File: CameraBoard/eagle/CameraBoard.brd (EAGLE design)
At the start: 101.6 x 76.2 mm, 86 parts, among them Q1 SI7465DP-T1-E3, Q2 BVSS123LT1G, Q3 BSS84, U1 MP26124GR-Z, U2 TPS63070, U3 LM2678SD-12/NOPB, U4 TS5A3159ADBVR, U5 ICM7242IBAZ-SMD, U6 H11F1SR2M, U7 H11F1SR2M, U8 SN74LVC1G17DCKR

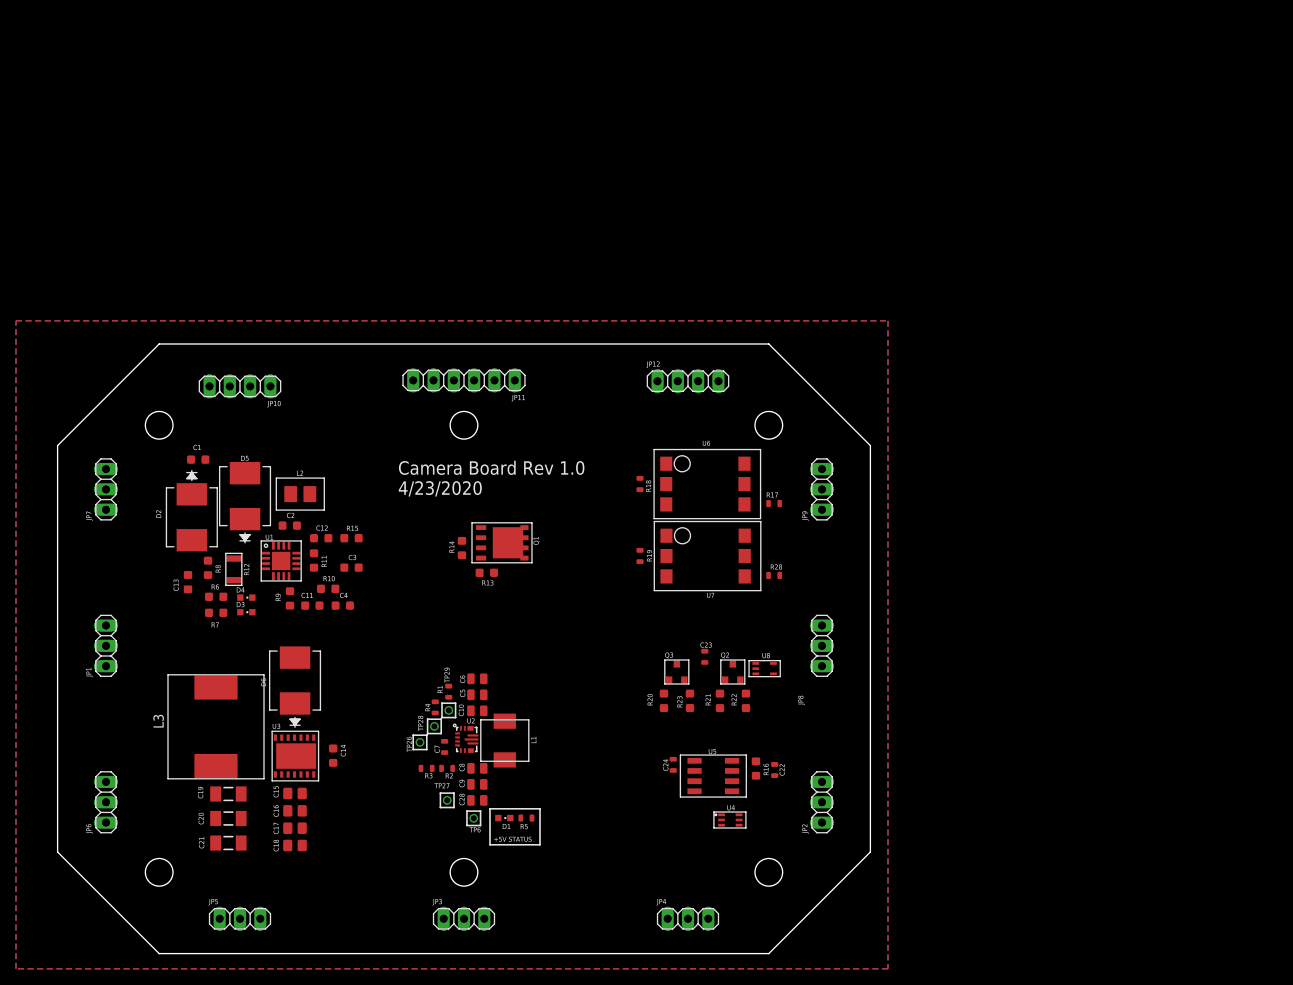
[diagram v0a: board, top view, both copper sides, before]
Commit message: finished board layout before routing
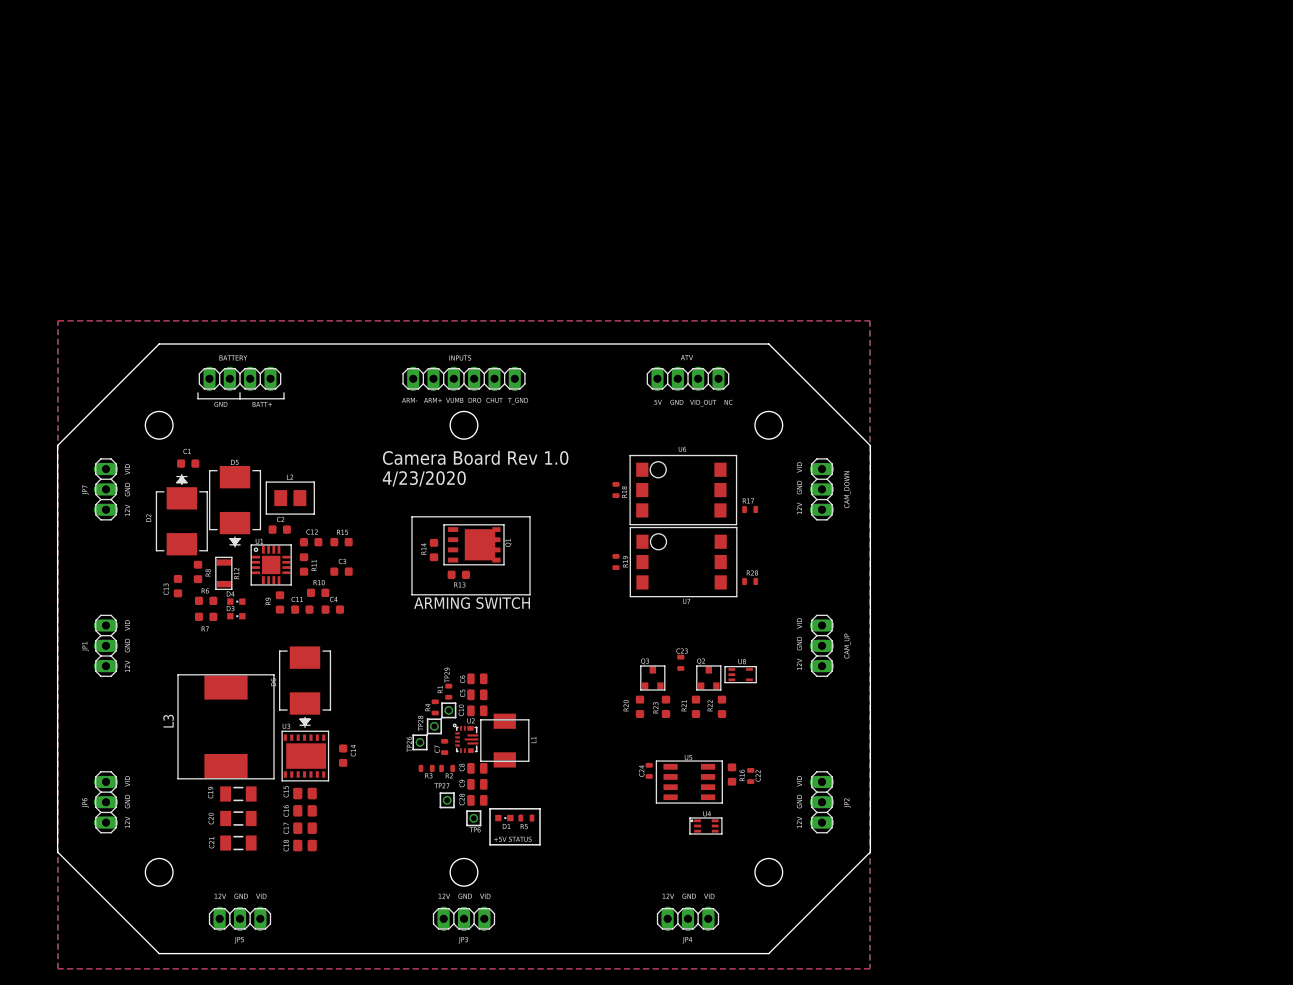
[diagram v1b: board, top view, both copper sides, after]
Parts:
- removed JP10, JP12: (no value), pinhead:1X04
- removed JP11: (no value), pinhead:1X06
- added ATV, BATTERY: (no value), pinhead:1X04
- added INPUTS: (no value), pinhead:1X06
- moved Q1 3.51 mm to (2.00, 13.0)
- moved R13 3.51 mm to (-0.65, 9.25)
- moved R14 3.51 mm to (-3.75, 12.3)
- moved C22 3.09 mm to (35.8, -15.9)
- moved C23 3.09 mm to (27.1, -1.75)
- moved C24 3.09 mm to (23.2, -15.3)
- moved Q2 3.09 mm to (30.6, -4.65)
- moved Q3 3.09 mm to (23.6, -4.65)
- moved R16 3.09 mm to (33.5, -15.7)
- moved R17 3.09 mm to (35.8, 17.4)
- moved R18 3.09 mm to (19.0, 19.9)
- moved R19 3.09 mm to (19.0, 10.8)
- moved R20 3.09 mm to (22.0, -7.25)
- moved R21 3.09 mm to (29.0, -7.25)
- moved R22 3.09 mm to (32.2, -7.25)
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- renumbered JP8 to CAM_UP, JP9 to CAM_DOWN
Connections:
- net +5V: now also ATV.1; no longer JP12.1
- net ARM-IN: now also INPUTS.6; no longer JP11.6
- net ARM-OUT: now also INPUTS.5; no longer JP11.5
- net BATT+: now also BATTERY.1, BATTERY.2; no longer JP10.1, JP10.2
- net CHUTE: now also INPUTS.2; no longer JP11.2
- net DROGUE: now also INPUTS.3; no longer JP11.3
- net GND: now also ATV.2, BATTERY.3, BATTERY.4; no longer JP10.3, JP10.4, JP12.2
- net T_GND: now also INPUTS.1; no longer JP11.1
- net VIDEO_OUT: now also ATV.3; no longer JP12.3
- net VUMB: now also INPUTS.4; no longer JP11.4
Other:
- board text added: "12V"
- board text added: "5V"
- board text added: "ARM+"
- board text added: "ARM-"
- board text added: "ARMING SWITCH"
- board text added: "BATT+"
- board text added: "CHUT"
- board text added: "DRO"
- board text added: "GND"
- board text added: "NC"
- board text added: "TO DO: -Massive L3 -Change JP ref designators to descriptive?"
- board text added: "T_GND"
- board text added: "VID"
- board text added: "VID_OUT"
- board text added: "VUMB"
- board text removed: "Armed Switch"
- board text removed: "TO DO: -Massive L3"

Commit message: completed routing of board rev 1.0
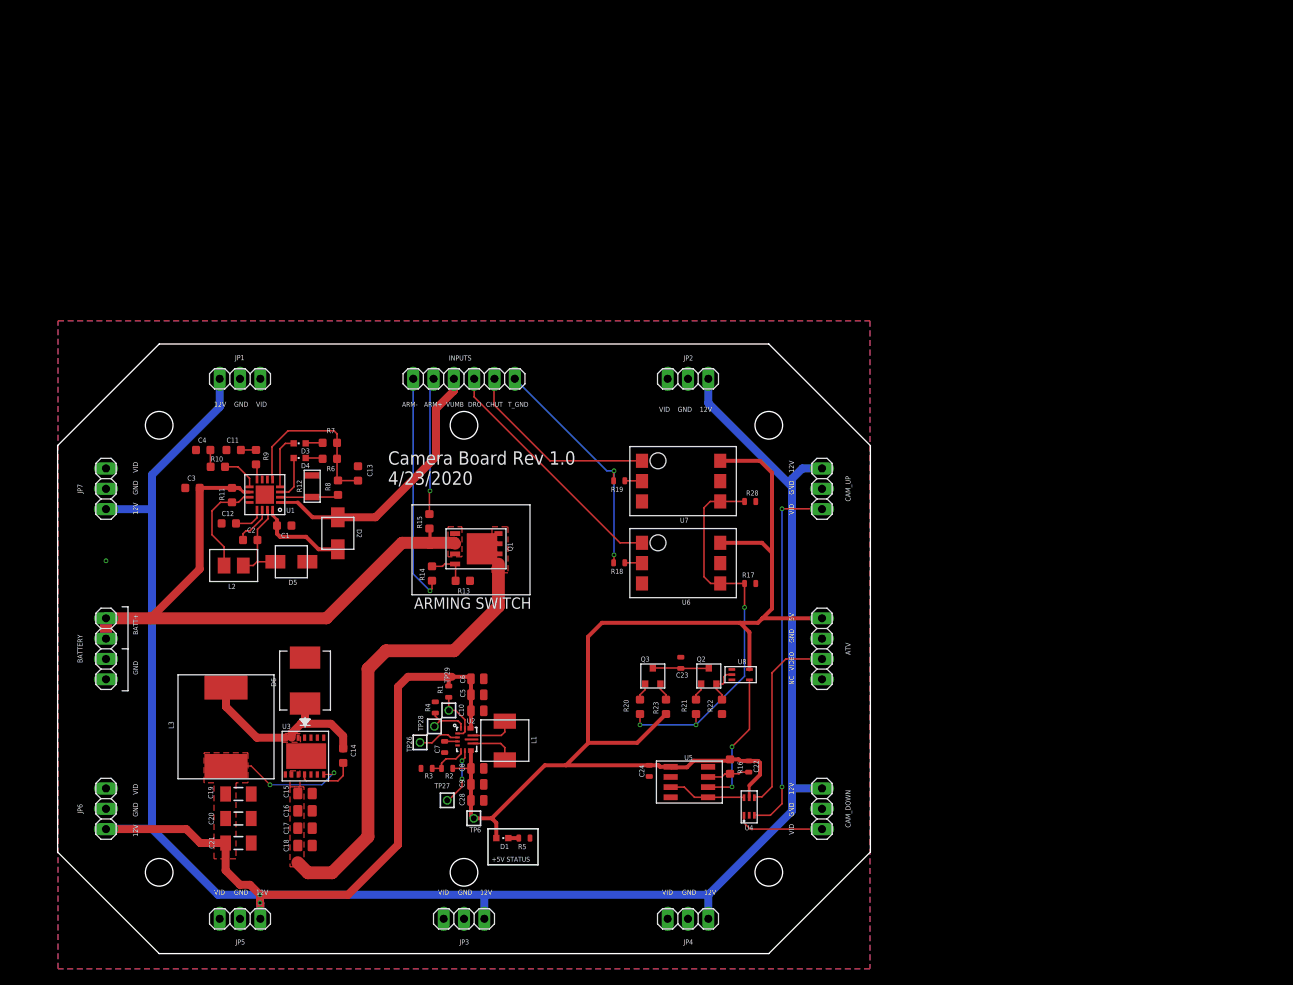
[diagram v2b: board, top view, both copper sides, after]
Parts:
- D2, D5: value D_MBRS340T3G -> S2MA-13-F; device D--MBRS340T3G--Schottky Diode:SMC -> D--S2MA-FDICT-ND--Schottky Diode 1.5A:S2MA-13-F
- moved JP2 55.5 mm to (28.0, 33.8), turned to 180 degrees
- moved CAM_DOWN 39.9 mm to (44.8, -20.0), turned to 270 degrees
- moved ATV 37.7 mm to (44.8, 0.00), turned to 270 degrees
- moved BATTERY 37.7 mm to (-44.8, 0.00), turned to 270 degrees
- moved JP1 37.3 mm to (-28.0, 33.8), turned to 0 degrees
- moved R7 26.7 mm to (-16.8, 25.8), turned to 0 degrees
- moved C13 26.5 mm to (-13.2, 21.9), turned to 90 degrees
- moved C4 25.7 mm to (-32.6, 24.9), turned to 180 degrees
- moved R6 23.5 mm to (-16.8, 23.8), turned to 0 degrees
- moved D3 23.0 mm to (-20.5, 25.7), turned to 90 degrees
- moved C11 21.7 mm to (-28.8, 24.9), turned to 180 degrees
- moved C3 21.4 mm to (-33.9, 20.1), turned to 180 degrees
- moved R8 20.4 mm to (-15.8, 20.1), turned to 90 degrees
- moved R10 20.1 mm to (-30.8, 22.8), turned to 180 degrees
- moved CAM_UP 19.6 mm to (44.8, 20.0), turned to 270 degrees
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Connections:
- net GND: now also D5.ANODE; no longer D5.2
- net N$15: now also D5.CATHODE; no longer D5.1
- net N$2: now also D2.CATHODE; no longer D2.1
- net VUMB: now also D2.ANODE; no longer D2.2
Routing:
- net +12V: track 0.00 -> 336.5 mm, vias 0 -> 4
- net +5V: track 0.00 -> 155.5 mm
- net BATT+: track 0.00 -> 77.3 mm
- net +16V: track 0.00 -> 57.0 mm
- net TIMERPULSE: track 0.00 -> 49.3 mm, vias 0 -> 3
- net CAM_UP: track 0.00 -> 45.9 mm, vias 0 -> 2
- net VUMB: track 0.00 -> 34.1 mm
- net DROGUE: track 0.00 -> 30.8 mm
- net T_GND: track 0.00 -> 30.0 mm, vias 0 -> 2
- net ARM-IN: track 0.00 -> 28.7 mm, vias 0 -> 1
- net CHUTE: track 0.00 -> 24.7 mm
- net VIDEO_OUT: track 0.00 -> 24.0 mm
- net 12V_OUT: track 0.00 -> 23.8 mm
- net N$4: track 0.00 -> 21.6 mm
- net TIMER_TRIGG: track 0.00 -> 17.3 mm, vias 0 -> 2
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- added copper zone on layer 1, net +12V
- added copper zone on layer 1, net +16V
- added copper zone on layer 1, net 12V_OUT
- added copper zone on layer 1, net BATT+
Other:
- board text added: "TO DO: -Massive L3 -is the polygon on the bypass caps for 12V SPS okay?"
- board text added: "VIDEO"
- board text removed: "TO DO: -Massive L3 -Change JP ref designators to descriptive?"
- board text removed: "VID_OUT"

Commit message: new image
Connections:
- net GND: now also R5.1
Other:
- board text added: "TO DO: -Massive L3 -is the polygon on the bypass caps for 12V SPS okay? -how to make nice GND stitching?"
- board text removed: "TO DO: -Massive L3 -is the polygon on the bypass caps for 12V SPS okay?"

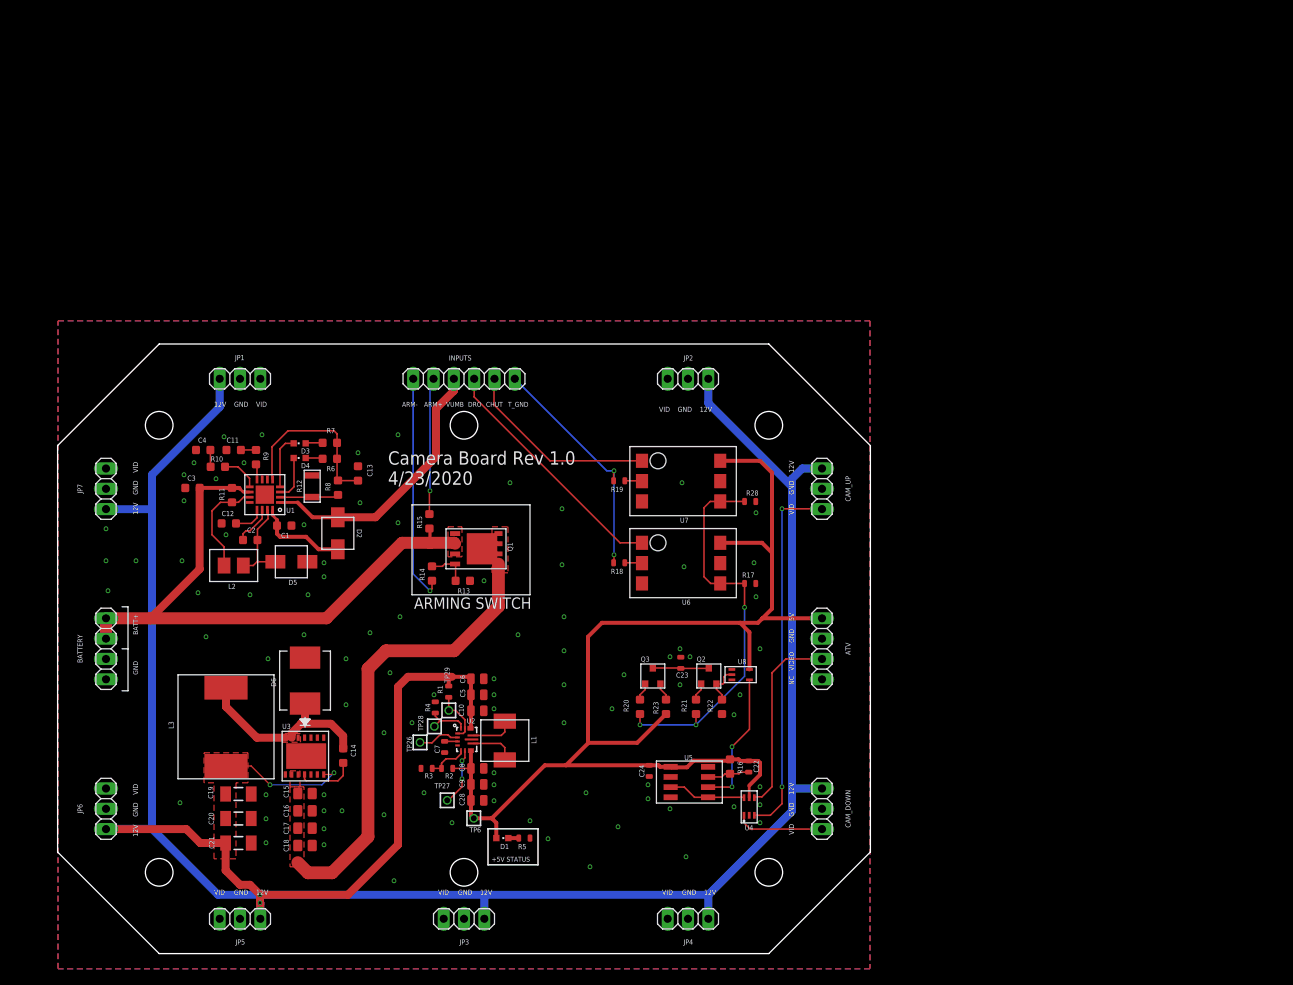
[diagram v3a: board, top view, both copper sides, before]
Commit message: added all the suggestions from first design review
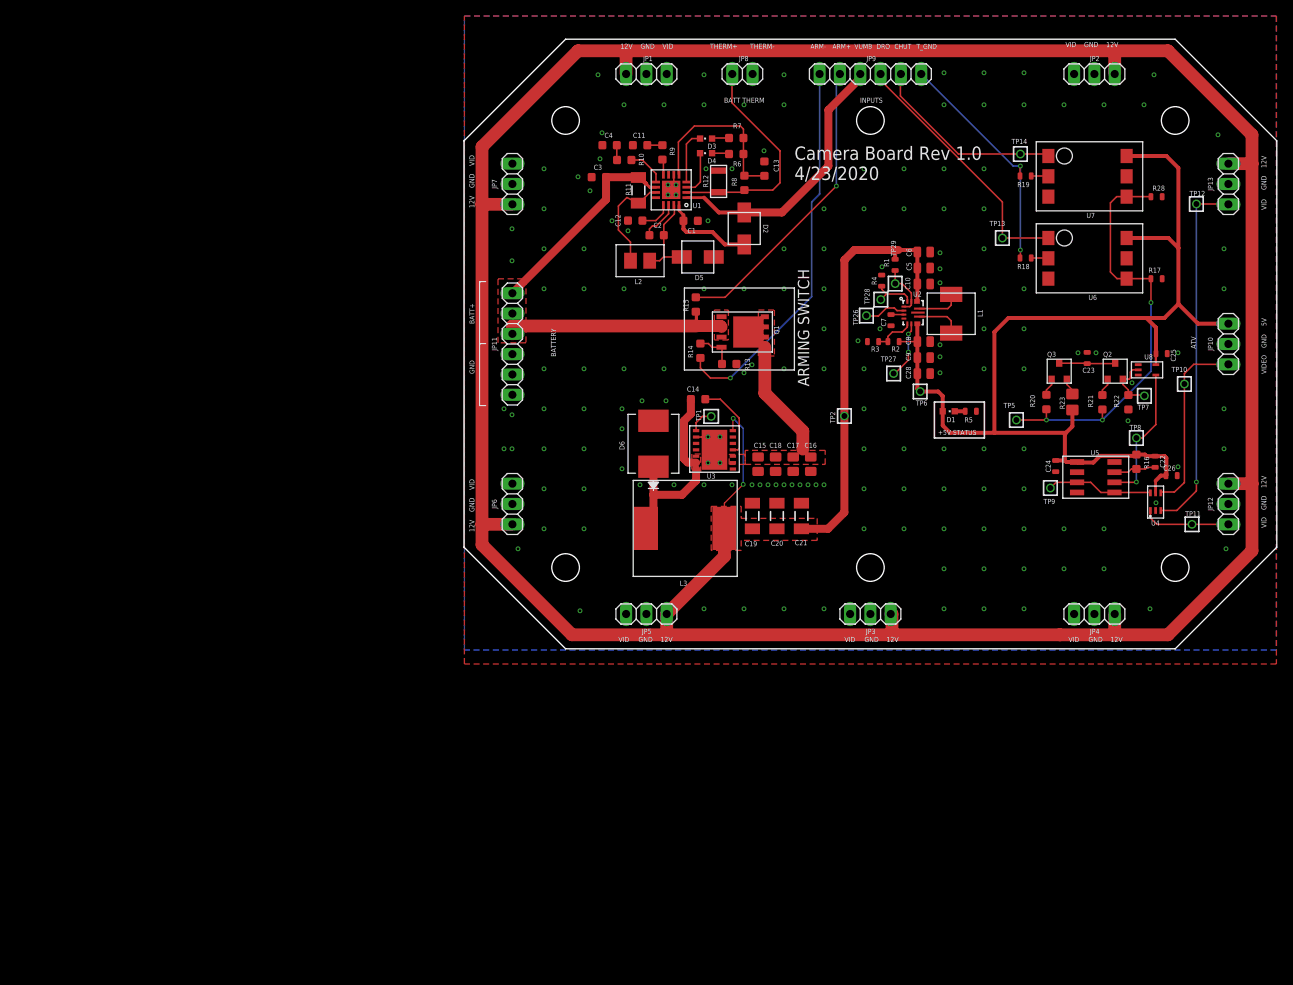
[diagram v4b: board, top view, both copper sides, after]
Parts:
- removed ATV, BATTERY: (no value), pinhead:1X04
- removed CAM_DOWN, CAM_UP: (no value), pinhead:1X03
- removed INPUTS: (no value), pinhead:1X06
- added C25, C26: 100n, oresat-rcl:.0603-C-NOSILK
- added JP10, JP12, JP13: (no value), pinhead:1X03
- added JP11, JP9: (no value), pinhead:1X06
- added JP8: (no value), pinhead:1X02
- added TP1, TP10, TP11, TP12, TP13, TP14, TP2, TP5, TP7, TP8, TP9: TEST-POINT, Tova:2MM-TEST-POINT
- C12, C2, C24: value 0.1u -> 100n
- C14: value 0.01u -> 10n
- L2: value 1239AS-H-100M=P2 -> 10uH
- R11: device oresat-rcl:.0603-A-NOSILK -> oresat-rcl:1206-A
- R13: value 1k -> 10k
- R23: device oresat-rcl:.0603-A-NOSILK -> oresat-rcl:.0805-A-NOSILK
- R5: value 221 -> 400
- moved C21 81.4 mm to (42.2, 16.6), turned to 90 degrees
- moved C20 77.2 mm to (39.1, 16.6), turned to 90 degrees
- moved C10 77.2 mm to (57.5, 45.6)
- moved C28 77.2 mm to (57.5, 34.4)
- moved C5 77.2 mm to (57.5, 47.6)
- moved C6 77.2 mm to (57.5, 49.6)
- moved C7 77.2 mm to (53.4, 41.1)
- moved C8 77.2 mm to (57.5, 38.4)
- moved C9 77.2 mm to (57.5, 36.4)
- moved D1 77.2 mm to (60.6, 29.7)
- moved L1 77.2 mm to (60.9, 41.9)
- moved R1 77.2 mm to (53.9, 48.0)
- moved R2 77.2 mm to (53.7, 38.4)
- moved R3 77.2 mm to (51.1, 38.4)
- moved R4 77.2 mm to (52.2, 46.0)
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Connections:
- net 12V_OUT renamed SOUT
- new net N$18: TP1.1, U3.8
- net !TIMER_OUTPUT: now also TP9.1
- net +12V: now also JP12.1, JP13.1, TP2.1; no longer CAM_DOWN.1, CAM_UP.1
- net +5V: now also C25.2, C26.2, JP10.1; no longer ATV.1
- net ARM-IN: now also JP9.6; no longer INPUTS.6
- net ARM-OUT: now also JP9.5; no longer INPUTS.5
- net BATT+: now also JP11.1, JP11.2, JP11.3; no longer BATTERY.1, BATTERY.2
- net CAM_DOWN: now also JP12.3, TP11.1; no longer CAM_DOWN.3
- net CAM_UP: now also JP13.3, TP12.1; no longer CAM_UP.3
- net CHUTE: now also JP9.2, TP14.1; no longer INPUTS.2
- net DROGUE: now also JP9.3, TP13.1; no longer INPUTS.3
- net GND: now also C25.1, C26.1, JP10.2, JP11.4, JP11.5, JP11.6, JP12.2, JP13.2, JP8.2, U1.EPAD, U3.DAP; no longer ATV.2, BATTERY.3, BATTERY.4, CAM_DOWN.2, CAM_UP.2
- net N$10: now also JP8.1
- net SCHMITTIN: now also TP7.1
- net TIMERPULSE: now also TP5.1
- net TIMER_TRIGG: now also TP8.1
- net T_GND: now also JP9.1; no longer INPUTS.1
- net VIDEO_OUT: now also JP10.3, TP10.1; no longer ATV.3
- net VUMB: now also JP9.4; no longer INPUTS.4
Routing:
- net +12V: track 336.5 -> 425.4 mm, vias 4 -> 2
- net +16V: track 57.0 -> 16.1 mm
- net BATT+: track 77.3 -> 55.1 mm
- net N$10: track 7.37 -> 28.3 mm
- net ARM-OUT: track 17.1 -> 37.5 mm
- net ARM-IN: track 28.7 -> 48.1 mm
- net +5V: track 155.5 -> 141.7 mm
- net GND: track 0.00 -> 5.00 mm, vias 1 -> 165
- net TIMERPULSE: track 49.3 -> 53.0 mm
- net !TIMER_OUTPUT: track 9.72 -> 13.3 mm
- net N$18: track 0.00 -> 3.21 mm
- net N$20: track 7.37 -> 9.87 mm
- net SCHMITTIN: track 5.10 -> 7.16 mm
- net DROGUE: track 30.8 -> 32.6 mm
- net SOUT: track 23.8 -> 25.1 mm
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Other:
- board text added: "ATV"
- board text added: "BATT THERM"
- board text added: "BATTERY"
- board text added: "INPUTS"
- board text added: "THERM+"
- board text added: "THERM-"
- board text removed: "NC"
